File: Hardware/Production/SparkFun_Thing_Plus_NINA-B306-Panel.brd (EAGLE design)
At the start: 22.9 x 66 mm, 145 parts, among them J1 USB-C, J2 THING_PLUS_LOGICAL, J3 CONN_03X2_NO4, J4 MICRO-SDFRICTION, J6 QWIIC_RA, Q1 20V/4.2A/52mΩ/1.4W, Q2 220mA/50V/3.5Ω, Q3 20V/4.2A/52mΩ/1.4W, U1 ESD Diode, U2 U-BLOX_NINA_B306, U3 XC6222B331MR-G, U4 MCP73831, U5 MAX17048, U6 ISM330DHCX, U7 BME280

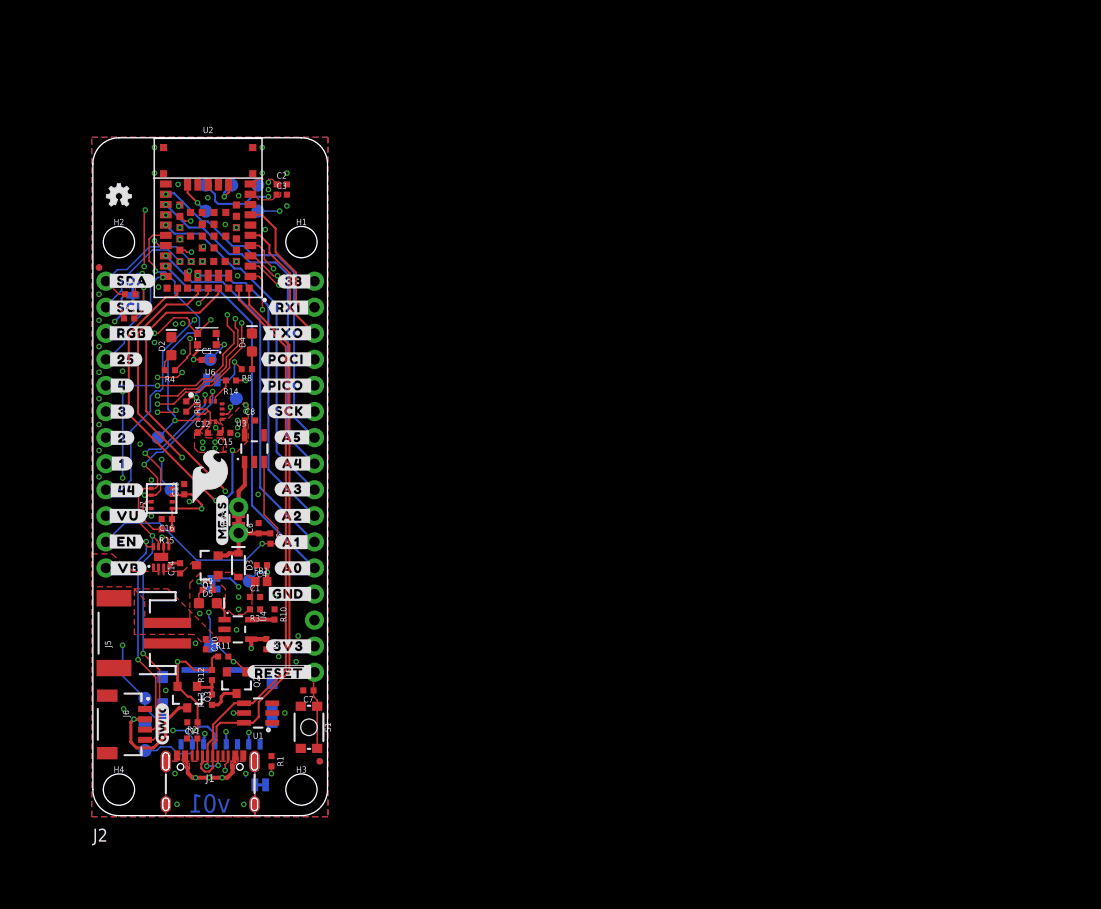
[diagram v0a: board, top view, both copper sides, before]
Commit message: routed and ready for v01 design review.
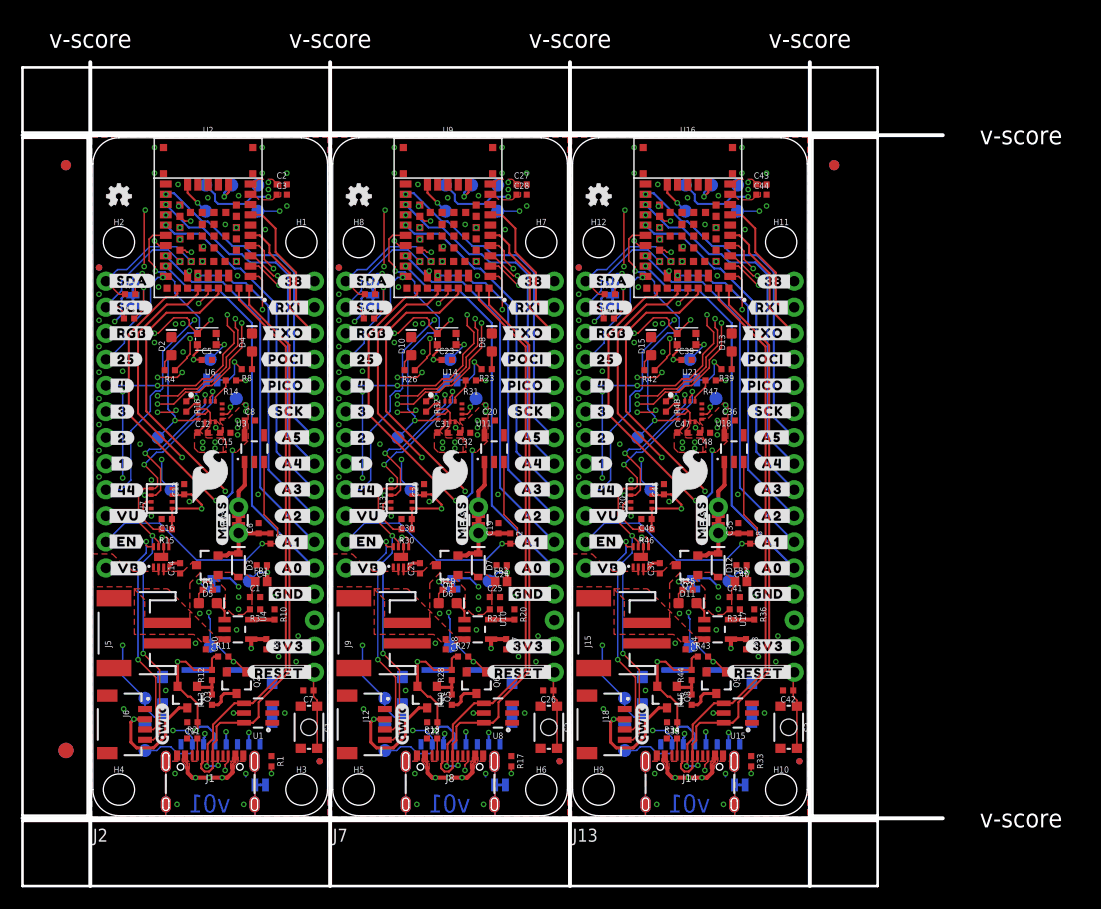
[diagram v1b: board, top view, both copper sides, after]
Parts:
- removed FRAME1: FRAME-LEDGER, SparkFun-Aesthetics:CREATIVE_COMMONS
- added C17, C18, C33, C34: 4.7uF, SparkFun-Capacitors:0402-TIGHT
- added C19, C35: 1.0uF, SparkFun-Capacitors:0402-TIGHT
- added C20, C36: 2.2uF, SparkFun-Capacitors:0402-TIGHT
- added C21, C23, C26, C27, C28, C29, C30, C31, C32, C37, C39, C42, C43, C44, C45, C46, C47, C48: 0.1uF, SparkFun-Capacitors:0402-TIGHT
- added C22, C38: 10uF, SparkFun-Capacitors:0402-TIGHT
- added C24, C25, C40, C41: 1.0nF, SparkFun-Capacitors:0402-TIGHT
- added CHG1, CHG2, PWR1, PWR2: JUMPER-SMT_2_NC_TRACE_SILK, SparkFun-Jumpers:SMT-JUMPER_2_NC_TRACE_SILK
- added D10, D15: BLUE, SparkFun-LED:LED-0603
- added D11, D6: Yellow, SparkFun-LED:LED-0603
- added D12, D7: 3A/10V/280mV, SparkFun-DiscreteSemi:SOD-323
- added D13, D8: RED, SparkFun-LED:LED-0603
- added D14, D9: WS2812, SparkFun-LED:WS2812-2020
- added E$1, E$2, E$3, E$4: (no value), SparkFun-Aesthetics:FIDUCIAL-1X2
- added E$5, E$6: (no value), SparkFun-Retired:FIDUCIAL-1.5X3
- added FB2, FB3: 120Ω, SparkFun-Coils:0402
- added FD10, FD11, FD12, FD5, FD6, FD7, FD8, FD9: FIDUCIALUFIDUCIAL, SparkFun-Aesthetics:FIDUCIAL-MICRO
- added H10, H11, H12, H5, H6, H7, H8, H9: STAND-OFFTIGHT, SparkFun-Hardware:STAND-OFF-TIGHT
- added I2C1, I2C2: JUMPER-SMT_3_2-NC_TRACE_SILK, SparkFun-Jumpers:SMT-JUMPER_3_2-NC_TRACE_SILK
- added J10, J16: MICRO-SDFRICTION, SparkFun-Connectors:MICROSD_TINY
- added J11, J17: CONN_03X2_NO4, MISC:PAD_05_03X2_TP_NO4
- added J12, J18: QWIIC_RA, SparkFun-Connectors:JST04_1MM_RA
- added J13, J7: THING_PLUS_LOGICAL, SparkFun-Boards:THING_PLUS
- added J14, J8: USB-C, SparkFun-Connectors:USB-C-16P-4LAYER-ISOLATED
- added J15, J9: (no value), SparkFun-Connectors:JST-2-SMD
- added LOGO10, LOGO15: FOUR_LAYER_WARNING, SparkFun-Aesthetics:FOUR_LAYER_WARNING
- added LOGO11, LOGO6: SFE_LOGO_NAME_FLAME.1_INCH, SparkFun-Aesthetics:SFE_LOGO_NAME_FLAME_.1
- added LOGO12, LOGO7: OSHW-LOGOMINI, SparkFun-Aesthetics:OSHW-LOGO-MINI
- added LOGO13, LOGO8: SPECIAL_INSTRUCTIONS-ORDERING, SparkFun-Aesthetics:ORDERING_INSTRUCTIONS
- added LOGO14, LOGO9: QWIIC_LOGO_4MM, SparkFun-Aesthetics:QWIIC_4MM
- added MEAS1, MEAS2: JUMPER-COMBO_2_NC_TRACE, SparkFun-Jumpers:COMBO-JUMPER_2_NC_TRACE
- added Q4, Q5, Q7, Q8: 20V/4.2A/52mΩ/1.4W, SparkFun-DiscreteSemi:SOT23-3
- added Q6, Q9: 220mA/50V/3.5Ω, SparkFun-DiscreteSemi:SOT23-3
- added R17, R18, R33, R34: 5.1k, SparkFun-Resistors:0402-TIGHT
- added R19, R35: 4.7k, SparkFun-Resistors:0402-TIGHT
- added R20, R36: 2.0K, SparkFun-Resistors:0402-TIGHT
- added R21, R22, R27, R28, R30, R31, R32, R37, R38, R43, R44, R46, R47, R48: 10k, SparkFun-Resistors:0402-TIGHT
- added R23, R39: 1k, SparkFun-Resistors:0402-TIGHT
- added R24, R25, R26, R40, R41, R42: 2.2k, SparkFun-Resistors:0402-TIGHT
- added R29, R45: 100, SparkFun-Resistors:0402-TIGHT
- added S2, S3: Reset, SparkFun-Switches:TACTILE_SWITCH_SMD_4.6X2.8MM
- added SHLD1, SHLD2: (no value), SparkFun-Jumpers:SMT-JUMPER_2_NC_TRACE_SILK
- added TP10, TP11, TP12, TP13, TP14, TP15, TP16, TP17, TP18, TP19, TP20, TP21, TP22, TP23, TP24, TP25, TP26, TP27: TEST-POINT3X5, SparkFun-Connectors:PAD.03X.05
- added U$100, U$162: (no value), output:#_SCK#71
- added U$101, U$163: (no value), output:#_PICO#72
- added U$102, U$164: (no value), output:#_POCI#73
- added U$103, U$165: (no value), output:#_TXO#74
- added U$104, U$166: (no value), output:#_RXI#75
- added U$105, U$167: (no value), output:#_38#76
- added U$106, U$168: (no value), output:#RGB_#78
- added U$107, U$169: (no value), output:#25_#79
- added U$108, U$170: (no value), output:#4_#79
- added U$109, U$171: (no value), output:#3_#79
- added U$110, U$172: (no value), output:#2_#79
- added U$111, U$173: (no value), output:#1_#79
- added U$112, U$174: (no value), output:#44_#79
- added U$113, U$175: (no value), output:#VUSB_#79
- added U$114, U$176: (no value), output:#EN_#80
- added U$115, U$177: (no value), output:#VBATT_#81
- added U$116, U$178: (no value), output:#SDA_#82
- added U$117, U$179: (no value), output:#SCL_#85
- added U$118, U$180: (no value), output:#_PWR#90
- added U$119, U$181: (no value), output:#CHG_#92
- added U$120, U$182: (no value), output:#_SHLD#93
- added U$121, U$183: (no value), output:SPARKFUN_THING_PLUS96
- added U$122, U$184: (no value), output:NINA#B30697
- added U$123, U$185: (no value), output:#_#RST##30698
- added U$124, U$186: (no value), output:#MEAS#30701
- added U$125, U$63: (no value), SparkFun-Aesthetics:SFE_LOGO_FLAME_STOP_.1
- added U$126, U$64: (no value), SparkFun-Aesthetics:SFE_LOGO_FLAME_.2
- added U$127, U$65: (no value), output:#_VB#46
- added U$128, U$66: (no value), output:#_EN#47
- added U$129, U$67: (no value), output:#_VU#48
- added U$130, U$68: (no value), output:#_44#49
- added U$131, U$69: (no value), output:#_1#49
- added U$132, U$70: (no value), output:#_2#49
- added U$133, U$71: (no value), output:#_3#49
- added U$134, U$72: (no value), output:#_4#49
- added U$135, U$73: (no value), output:#_25#49
- added U$136, U$74: (no value), output:#_SCL#49
- added U$137, U$75: (no value), output:##RESET#_#52
- added U$138, U$76: (no value), output:#GND_#53
- added U$139, U$77: (no value), output:#A0_#54
- added U$140, U$78: (no value), output:#A1_#54
- added U$141, U$79: (no value), output:#A2_#54
- added U$142, U$80: (no value), output:#A3_#54
- added U$143, U$81: (no value), output:#A4_#54
- added U$144, U$82: (no value), output:#A5_#54
- added U$145, U$83: (no value), output:#SCK_#54
- added U$146, U$84: (no value), output:#TXO_#57
- added U$147, U$85: (no value), output:#RXI_#59
- added U$148, U$86: (no value), output:#38_#60
- added U$149, U$87: (no value), output:#PICO_#60
- added U$150, U$88: (no value), output:#POCI_#61
- added U$151, U$89: (no value), output:#_RGB#64
- added U$152, U$90: (no value), output:#3V3_#65
- added U$153, U$91: (no value), output:#_SDA#68
- added U$154, U$92: (no value), output:#_3V3#70
- added U$155, U$93: (no value), output:#_GND#70
- added U$156, U$94: (no value), output:#_A0#71
- added U$157, U$95: (no value), output:#_A1#71
- added U$158, U$96: (no value), output:#_A2#71
- added U$159, U$97: (no value), output:#_A3#71
- added U$160, U$98: (no value), output:#_A4#71
- added U$161, U$99: (no value), output:#_A5#71
- added U10, U17: MCP73831, SparkFun-IC-Power:SOT23-5
- added U11, U18: XC6222B331MR-G, SparkFun-IC-Power:SOT23-5
- added U12, U19: MAX17048, SparkFun-IC-Power:DFN-8
- added U13, U20: BME280, SparkFun-Sensors:LGA-8-2.5X2.5
- added U14, U21: ISM330DHCX, SparkFun-Sensors:LGA-14L
- added U15, U8: ESD Diode, SparkFun-DiscreteSemi:SOT-23-6
- added U16, U9: U-BLOX_NINA_B306, U-BLOX_NINA_B306:NINA_B306
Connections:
- new net !RESET!1: C26.1, J11.6, J7.28, S2.3, S2.4, U9.19
- new net !RESET!2: C42.1, J13.28, J17.6, S3.3, S3.4, U16.19
- new net 3.3V1: C20.1, C22.1, C23.1, C27.1, C28.1, C29.1, C30.1, C31.1, C32.1, D9.VCC, I2C1.2, J10.4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
- new net 3.3V2: C36.1, C38.1, C39.1, C43.1, C44.1, C45.1, C46.1, C47.1, C48.1, D14.VCC, I2C2.2, J13.27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
- new net 3V3_QWIIC1: J12.2, Q5.3, TP18.1
- new net 3V3_QWIIC2: J18.2, Q8.3, TP27.1
- new net EN1: J7.11, R22.2, U11.3
- new net EN2: J13.11, R38.2, U18.3
- new net GND1: C17.2, C18.2, C19.2, C20.2, C21.2, C22.2, C23.2, C24.2, C25.2, C26.2, C27.2, C28.2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
- new net GND2: C33.2, C34.2, C35.2, C36.2, C37.2, C38.2, C39.2, C40.2, C41.2, C42.2, C43.2, C44.2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
- new net IO1/GPIO2: J7.8, U9.1
- new net IO1/GPIO3: J13.8, U16.1
- new net IO17/A1: J7.19, U9.17
- new net IO17/A2: J13.19, U16.17
- new net IO18/A1: J7.20, U9.18
- new net IO18/A2: J13.20, U16.18
- new net IO2/GPIO1: J7.7, U9.2
- new net IO2/GPIO3: J13.7, U16.2
- new net IO20/A1: J7.21, U9.20
- new net IO20/A2: J13.21, U16.20
- new net IO21/IMU_INT2: TP14.1, U14.P4, U9.21
- new net IO21/IMU_INT3: TP23.1, U16.21, U21.P4
- new net IO22/IMU_INT1: TP15.1, U14.P9, U9.22
- new net IO22/IMU_INT3: TP24.1, U16.22, U21.P9
- new net IO23/A2: J7.23, U9.23
- new net IO23/A3: J13.23, U16.23
- new net IO24/A1: J7.24, U9.24
- new net IO24/A2: J13.24, U16.24
- new net IO25/GPIO1: J7.4, U9.25
- new net IO25/GPIO2: J13.4, U16.25
- new net IO27/A1: J7.22, U9.27
- new net IO27/A3: J13.22, U16.27
- new net IO3/GPIO1: J7.6, U9.3
- new net IO3/GPIO2: J13.6, U16.3
- new net IO34/GPIO6/RGB1: D9.DI, J7.3, U9.34
- new net IO34/GPIO6/RGB2: D14.DI, J13.3, U16.34
- new net IO37/SD_DET1: J10.9, TP12.1, U9.37
- new net IO37/SD_DET2: J16.9, TP21.1, U16.37
- new net IO38/FREE1: J7.13, U9.38
- new net IO38/FREE2: J13.13, U16.38
- new net IO39/!BATT_ALRT!1: TP16.1, U12.5, U9.39
- new net IO39/!BATT_ALRT!2: TP25.1, U16.39, U19.5
- new net IO4/GPIO1: J7.5, U9.4
- new net IO4/GPIO2: J13.5, U16.4
- new net IO40/QWIIC_PEN1: Q6.1, R27.2, TP13.1, U9.40
- new net IO40/QWIIC_PEN2: Q9.1, R43.2, TP22.1, U16.40
- new net IO41/LED1: R26.1, U9.41
- new net IO41/LED2: R42.1, U16.41
- new net IO42/SCL1: J12.4, J7.2, R24.1, U12.7, U13.4, U14.P13, U9.42
- new net IO42/SCL2: J13.2, J18.4, R40.1, U16.42, U19.7, U20.4, U21.P13
- new net IO43/SDA1: J12.3, J7.1, R25.1, U12.8, U13.3, U14.P14, U9.43
- new net IO43/SDA2: J13.1, J18.3, R41.1, U16.43, U19.8, U20.3, U21.P14
- new net IO44/GPIO1: J7.9, U9.44
- new net IO44/GPIO2: J13.9, U16.44
- new net IO48/POCI1: J10.7, J7.16, U9.48
- new net IO48/POCI2: J13.16, J16.7, U16.48
- new net IO5/NINA_RX/DEV_TX1: J7.15, U9.5
- new net IO5/NINA_RX/DEV_TX2: J13.15, U16.5
- new net IO50/PICO1: J10.3, J7.17, U9.50
- new net IO50/PICO2: J13.17, J16.3, U16.50
- new net IO51/SD_!CS!1: J10.2, TP10.1, U9.51
- new net IO51/SD_!CS!2: J16.2, TP19.1, U16.51
- new net IO52/SCK1: J10.5, J7.18, U9.52
- new net IO52/SCK2: J13.18, J16.5, U16.52
- new net IO7/NINA_TX/DEV_RX1: J7.14, U9.7
- new net IO7/NINA_TX/DEV_RX2: J13.14, U16.7
- new net N$12: J8.B5, R17.2
- new net N$17: J8.A5, R18.2
- new net N$21: D6.C, U10.1
- new net N$22: D6.A, R19.1
- new net N$23: CHG1.1, R19.2
- new net N$24: R20.2, U10.5
- new net N$25: D8.A, R23.1
- new net N$26: PWR1.1, R23.2
- new net N$27: D9.DO, TP11.1
- new net N$28: C24.1, FB2.2, TP17.1, U9.31
- new net N$29: D10.A, R26.2
- new net N$30: Q6.3, R29.1
- new net N$31: R30.2, U13.2
- new net N$32: R31.2, U14.P12
- new net N$33: R32.2, U14.P1
- new net N$34: Q5.1, R28.1, R29.2
- new net N$35: C19.1, D7.C, MEAS1.1, MEAS1.3, Q4.2, R22.1
- new net N$37: J14.B5, R33.2
- new net N$38: J14.A5, R34.2
- new net N$39: D11.C, U17.1
- new net N$40: D11.A, R35.1
- new net N$41: CHG2.1, R35.2
- new net N$42: R36.2, U17.5
- new net N$43: D13.A, R39.1
- new net N$44: PWR2.1, R39.2
- new net N$45: D14.DO, TP20.1
- new net N$46: C40.1, FB3.2, TP26.1, U16.31
- new net N$47: D15.A, R42.2
- new net N$48: Q9.3, R45.1
- new net N$49: R46.2, U20.2
- new net N$50: R47.2, U21.P12
- new net N$51: R48.2, U21.P1
- new net N$52: Q8.1, R44.1, R45.2
- new net N$53: C35.1, D12.C, MEAS2.1, MEAS2.3, Q7.2, R38.1
- new net SCL_PU_PWR1: I2C1.3, R24.2
- new net SCL_PU_PWR2: I2C2.3, R40.2
- new net SDA_PU_PWR1: I2C1.1, R25.2
- new net SDA_PU_PWR2: I2C2.1, R41.2
- new net SHLD1: J8.SHLD1, J8.SHLD2, J8.SHLD3, J8.SHLD4, J8.SHLD5, J8.SHLD6, J8.SHLD7, J8.SHLD8, SHLD1.2
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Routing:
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- added copper zone on layer 1, net 3.3V1
- added copper zone on layer 15, net 3.3V1
- added copper zone on layer 1, net 3.3V2
- added copper zone on layer 15, net 3.3V2
- added copper zone on layer 1, net GND1
- added copper zone on layer 16, net GND1
- added copper zone on layer 2, net GND1
- added copper zone on layer 1, net GND2
- added copper zone on layer 16, net GND2
- added copper zone on layer 2, net GND2
- added copper zone on layer 1, net SHLD1
- added copper zone on layer 16, net SHLD1
- added copper zone on layer 2, net SHLD1
- added copper zone on layer 1, net SHLD2
- added copper zone on layer 16, net SHLD2
- added copper zone on layer 2, net SHLD2
- added copper zone on layer 1, net V_BATT1
- added copper zone on layer 1, net V_BATT2
- added copper zone on layer 1, net V_USB1
- added copper zone on layer 15, net V_USB1
- added copper zone on layer 1, net V_USB2
- added copper zone on layer 15, net V_USB2
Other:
- board size 22.9 x 66 mm -> 89.7 x 80.3 mm
- board text added: "v-score"
- board text removed: "Alex Brudner"
- board text removed: "All measurements in inches."

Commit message: v01 ready for production.
Move Power LED
Move MEAS jumper
Move GPIO6 to a new IO pin
Remove Q2
Allow ground pour between IO41 and SDA
Add vias next to BME280 ground pad
Shorten !RESET! top silk to !RST!
Swap CHG silk vertical direction
Add IMU silk from ISM BOB
Add more ground vias
Rotate !RST! on bottom silk
Reset button silk
LED silk
Add "NINA-B306" under module on top silk
Align LEDs vertically
Evenly space LEDs horizontally
Reroute
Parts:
- removed Q7, Q8: 20V/4.2A/52mΩ/1.4W, SparkFun-DiscreteSemi:SOT23-3
- removed Q9: 220mA/50V/3.5Ω, SparkFun-DiscreteSemi:SOT23-3
- removed R43, R44, R46, R47, R48: 10k, SparkFun-Resistors:0402-TIGHT
- removed R45: 100, SparkFun-Resistors:0402-TIGHT
- added U$187: (no value), output:#RGB_#78
- added U$188: (no value), output:#25_#79
- added U$189: (no value), output:#4_#79
- added U$190: (no value), output:#3_#79
- added U$191: (no value), output:#2_#79
- added U$192: (no value), output:#1_#79
- added U$193: (no value), output:#44_#79
- added U$194: (no value), output:#VUSB_#79
- added U$195: (no value), output:#EN_#80
- added U$196: (no value), output:#VBATT_#81
- added U$197: (no value), output:#SDA_#82
- added U$198: (no value), output:#SCL_#85
- added U$199: (no value), output:#_PWR#90
- added U$200: (no value), output:#_SHLD#93
- added U$201: (no value), output:SPARKFUN_THING_PLUS96
- added U$202: (no value), output:NINA#B30697
- added U$203: (no value), output:#MEAS#30701
- added U$204: (no value), output:##RST#_#30704
- added U$205: (no value), output:#_#RST##30705
- added U$206: (no value), output:#_CHG#30707
- added U$207: (no value), output:##RESET##30708
- added U$208: (no value), output:RGB30710
- added U$209: (no value), output:STAT30711
- added U$210: (no value), output:PWR30712
- added U$211: (no value), output:NINA#B30630713
- added U$212: (no value), ISMTopMini:X2114
- added U$213: (no value), ISMTopMini:Y2115
- added U$214: (no value), ISMTopMini:Z2116
- added U$215: (no value), output:IO414130630715
- added U$216: (no value), output:IO34414130630716
- D10, D15: value BLUE -> RED
- D13, D8: value RED -> WS2812; device SparkFun-LED:LED-0603 -> SparkFun-LED:WS2812-2020
- D14, D9: value WS2812 -> BLUE; device SparkFun-LED:WS2812-2020 -> SparkFun-LED:LED-0603
- Q2, Q6: value 220mA/50V/3.5Ω -> 20V/4.2A/52mΩ/1.4W
- R11, R30: value 10k -> 5.1k
- R13, R29: value 100 -> 5.1k
- R17: value 5.1k -> 4.7k
- R18: value 5.1k -> 2.0K
- R19: value 4.7k -> 10k
- R20: value 2.0K -> 10k
- R21, R22, R37: value 10k -> 2.2k
- R23: value 1k -> 2.2k
- R24, R25, R26, R40, R41: value 2.2k -> 10k
- R28: value 10k -> 1k
- R31: value 10k -> 4.7k
- R32: value 10k -> 2.0K
- R33, R34: value 5.1k -> 10k
- R35: value 4.7k -> 2.2k
- R36: value 2.0K -> 2.2k
- R39: value 1k -> 10k
- R42: value 2.2k -> 1k
- U$100: device output:#_SCK#71 -> output:#_SDA#68
- U$101: device output:#_PICO#72 -> output:#_3V3#70
- U$102: device output:#_POCI#73 -> output:#_GND#70
- U$103: device output:#_TXO#74 -> output:#_A0#71
- U$104: device output:#_RXI#75 -> output:#_A1#71
- U$105: device output:#_38#76 -> output:#_A2#71
- U$106: device output:#RGB_#78 -> output:#_A3#71
- U$107: device output:#25_#79 -> output:#_A4#71
- U$108: device output:#4_#79 -> output:#_A5#71
- U$109: device output:#3_#79 -> output:#_SCK#71
- U$110: device output:#2_#79 -> output:#_PICO#72
- U$111: device output:#1_#79 -> output:#_POCI#73
- U$112: device output:#44_#79 -> output:#_TXO#74
- U$113: device output:#VUSB_#79 -> output:#_RXI#75
- U$114: device output:#EN_#80 -> output:#_38#76
- U$115: device output:#VBATT_#81 -> output:#RGB_#78
- U$116: device output:#SDA_#82 -> output:#25_#79
- U$117: device output:#SCL_#85 -> output:#4_#79
- U$118: device output:#_PWR#90 -> output:#3_#79
- U$119: device output:#CHG_#92 -> output:#2_#79
- U$120: device output:#_SHLD#93 -> output:#1_#79
- U$121: device output:SPARKFUN_THING_PLUS96 -> output:#44_#79
- U$122: device output:NINA#B30697 -> output:#VUSB_#79
- U$123: device output:#_#RST##30698 -> output:#EN_#80
- U$124: device output:#MEAS#30701 -> output:#VBATT_#81
- U$125: device SparkFun-Aesthetics:SFE_LOGO_FLAME_STOP_.1 -> output:#SDA_#82
- U$126: device SparkFun-Aesthetics:SFE_LOGO_FLAME_.2 -> output:#SCL_#85
- U$127: device output:#_VB#46 -> output:#_PWR#90
- U$128: device output:#_EN#47 -> output:#_SHLD#93
- U$129: device output:#_VU#48 -> output:SPARKFUN_THING_PLUS96
- U$130: device output:#_44#49 -> output:NINA#B30697
- U$131: device output:#_1#49 -> output:#MEAS#30701
- U$132: device output:#_2#49 -> output:##RST#_#30704
- U$133: device output:#_3#49 -> output:#_#RST##30705
- U$134: device output:#_4#49 -> output:#_CHG#30707
- U$135: device output:#_25#49 -> output:##RESET##30708
- U$136: device output:#_SCL#49 -> output:RGB30710
- U$137: device output:##RESET#_#52 -> output:STAT30711
- U$138: device output:#GND_#53 -> output:PWR30712
- U$139: device output:#A0_#54 -> output:NINA#B30630713
- U$140: device output:#A1_#54 -> ISMTopMini:X2114
- U$141: device output:#A2_#54 -> ISMTopMini:Y2115
- U$142: device output:#A3_#54 -> ISMTopMini:Z2116
- U$143: device output:#A4_#54 -> output:IO414130630715
- U$144: device output:#A5_#54 -> output:IO34414130630716
- U$145: device output:#SCK_#54 -> SparkFun-Aesthetics:SFE_LOGO_FLAME_STOP_.1
- U$146: device output:#TXO_#57 -> SparkFun-Aesthetics:SFE_LOGO_FLAME_.2
- U$147: device output:#RXI_#59 -> output:#_VB#46
- U$148: device output:#38_#60 -> output:#_EN#47
- U$149: device output:#PICO_#60 -> output:#_VU#48
- U$15: device output:##RESET#_#52 -> output:##RST#_#30704
- U$150: device output:#POCI_#61 -> output:#_44#49
- U$151: device output:#_RGB#64 -> output:#_1#49
- U$152: device output:#3V3_#65 -> output:#_2#49
- U$153: device output:#_SDA#68 -> output:#_3#49
- U$154: device output:#_3V3#70 -> output:#_4#49
- U$155: device output:#_GND#70 -> output:#_25#49
- U$156: device output:#_A0#71 -> output:#_SCL#49
- U$157: device output:#_A1#71 -> output:#GND_#53
- U$158: device output:#_A2#71 -> output:#A0_#54
- U$159: device output:#_A3#71 -> output:#A1_#54
- U$160: device output:#_A4#71 -> output:#A2_#54
- U$161: device output:#_A5#71 -> output:#A3_#54
- U$162: device output:#_SCK#71 -> output:#A4_#54
- U$163: device output:#_PICO#72 -> output:#A5_#54
- U$164: device output:#_POCI#73 -> output:#SCK_#54
- U$165: device output:#_TXO#74 -> output:#TXO_#57
- U$166: device output:#_RXI#75 -> output:#RXI_#59
- U$167: device output:#_38#76 -> output:#38_#60
- U$168: device output:#RGB_#78 -> output:#PICO_#60
- U$169: device output:#25_#79 -> output:#POCI_#61
- U$170: device output:#4_#79 -> output:#_RGB#64
- U$171: device output:#3_#79 -> output:#3V3_#65
- U$172: device output:#2_#79 -> output:#_SDA#68
- U$173: device output:#1_#79 -> output:#_3V3#70
- U$174: device output:#44_#79 -> output:#_GND#70
- U$175: device output:#VUSB_#79 -> output:#_A0#71
- U$176: device output:#EN_#80 -> output:#_A1#71
- U$177: device output:#VBATT_#81 -> output:#_A2#71
- U$178: device output:#SDA_#82 -> output:#_A3#71
- U$179: device output:#SCL_#85 -> output:#_A4#71
- U$180: device output:#_PWR#90 -> output:#_A5#71
- U$181: device output:#CHG_#92 -> output:#_SCK#71
- U$182: device output:#_SHLD#93 -> output:#_PICO#72
- U$183: device output:SPARKFUN_THING_PLUS96 -> output:#_POCI#73
- U$184: device output:NINA#B30697 -> output:#_TXO#74
- U$185: device output:#_#RST##30698 -> output:#_RXI#75
- U$186: device output:#MEAS#30701 -> output:#_38#76
- U$30: device output:#_#RST##30698 -> output:#_CHG#30707
- U$58: device output:#CHG_#92 -> output:##RESET##30708
- U$63: device SparkFun-Aesthetics:SFE_LOGO_FLAME_STOP_.1 -> output:#_#RST##30705
- U$64: device SparkFun-Aesthetics:SFE_LOGO_FLAME_.2 -> output:RGB30710
- U$65: device output:#_VB#46 -> output:STAT30711
- U$66: device output:#_EN#47 -> output:PWR30712
- U$67: device output:#_VU#48 -> output:NINA#B30630713
- U$68: device output:#_44#49 -> ISMTopMini:X2114
- U$69: device output:#_1#49 -> ISMTopMini:Y2115
- U$70: device output:#_2#49 -> ISMTopMini:Z2116
- U$71: device output:#_3#49 -> output:IO414130630715
- U$72: device output:#_4#49 -> output:IO34414130630716
- U$73: device output:#_25#49 -> SparkFun-Aesthetics:SFE_LOGO_FLAME_STOP_.1
- U$74: device output:#_SCL#49 -> SparkFun-Aesthetics:SFE_LOGO_FLAME_.2
- U$75: device output:##RESET#_#52 -> output:#_VB#46
- U$76: device output:#GND_#53 -> output:#_EN#47
- U$77: device output:#A0_#54 -> output:#_VU#48
- U$78: device output:#A1_#54 -> output:#_44#49
- U$79: device output:#A2_#54 -> output:#_1#49
- U$80: device output:#A3_#54 -> output:#_2#49
- U$81: device output:#A4_#54 -> output:#_3#49
- U$82: device output:#A5_#54 -> output:#_4#49
- U$83: device output:#SCK_#54 -> output:#_25#49
- U$84: device output:#TXO_#57 -> output:#_SCL#49
- U$85: device output:#RXI_#59 -> output:#GND_#53
- U$86: device output:#38_#60 -> output:#A0_#54
- U$87: device output:#PICO_#60 -> output:#A1_#54
- U$88: device output:#POCI_#61 -> output:#A2_#54
- U$89: device output:#_RGB#64 -> output:#A3_#54
- U$90: device output:#3V3_#65 -> output:#A4_#54
- U$91: device output:#_SDA#68 -> output:#A5_#54
- U$92: device output:#_3V3#70 -> output:#SCK_#54
- U$93: device output:#_GND#70 -> output:#TXO_#57
- U$94: device output:#_A0#71 -> output:#RXI_#59
- U$95: device output:#_A1#71 -> output:#38_#60
- U$96: device output:#_A2#71 -> output:#PICO_#60
- U$97: device output:#_A3#71 -> output:#POCI_#61
- U$98: device output:#_A4#71 -> output:#_RGB#64
- U$99: device output:#_A5#71 -> output:#3V3_#65
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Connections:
- removed net IO34/GPIO6/RGB: D1.DI, J2.3, U2.34
- removed net IO34/GPIO6/RGB1: D9.DI, J7.3, U9.34
- removed net IO34/GPIO6/RGB2: D14.DI, J13.3, U16.34
- removed net IO40/QWIIC_PEN: Q2.1, R11.2, TP5.1, U2.40
- removed net IO40/QWIIC_PEN1: Q6.1, R27.2, TP13.1, U9.40
- removed net IO40/QWIIC_PEN2: Q9.1, R43.2, TP22.1, U16.40
- removed net N$23 (its old number): CHG1.1, R19.2
- removed net N$33 (its old number): R32.2, U14.P1
- removed net N$38 (its old number): J14.A5, R34.2
- removed net N$47: D15.A, R42.2
- removed net N$48: Q9.3, R45.1
- removed net N$49: R46.2, U20.2
- removed net N$50: R47.2, U21.P12
- removed net N$51: R48.2, U21.P1
- removed net N$52: Q8.1, R44.1, R45.2
- removed net N$53: C35.1, D12.C, MEAS2.1, MEAS2.3, Q7.2, R38.1
- new net IO34/RGB: D1.DI, U2.34
- new net IO34/RGB1: D8.DI, U9.34
- new net IO34/RGB2: D13.DI, U16.34
- new net IO35/GPIO1: J7.3, U9.35
- new net IO35/GPIO2: J13.3, U16.35
- new net IO35/GPIO6: J2.3, U2.35
- new net IO40/QWIIC_!PEN!: Q3.1, R12.2, TP5.1, U2.40
- new net IO40/QWIIC_!PEN!1: Q4.1, R24.2, TP13.1, U9.40
- new net IO40/QWIIC_!PEN!2: Q6.1, R38.2, TP22.1, U16.40
- new net N$21: R18.2, U10.5
- new net N$28: PWR1.1, R28.2
- new net N$36: R32.2, U17.5
- new net N$39: D14.A, R37.2
- net 3.3V: no longer R11.1, R12.2
- net 3.3V1: now also D8.VCC, Q4.2, R25.1, R26.1; no longer D9.VCC, Q5.2, R28.2, R30.1, R31.1, R32.1
- net 3.3V2: now also D13.VCC, Q6.2, R39.1, R40.1, R41.1; no longer D14.VCC, Q8.2, R43.1, R44.2, R46.1, R47.1, R48.1
- net 3V3_QWIIC1: now also Q4.3; no longer Q5.3
- net 3V3_QWIIC2: now also Q6.3; no longer Q8.3
- net EN1: now also R20.2; no longer R22.2
- net EN2: now also R34.2; no longer R38.2
- net GND: now also R12.1; no longer Q2.2
- net GND1: now also D8.GND, D9.C, R11.1, R13.1, R19.1, R24.1; no longer D8.C, D9.GND, Q6.2, R17.1, R20.1, R21.1
- net GND2: now also D13.GND, D14.C, R29.1, R30.1, R32.1, R38.1; no longer D13.C, D14.GND, Q9.2, R34.1, R36.1, R37.1
- net IO41/LED1: now also R23.1; no longer R26.1
- net IO41/LED2: now also R37.1; no longer R42.1
- net IO42/SCL1: now also R21.1; no longer R24.1
- net IO42/SCL2: now also R35.1; no longer R40.1
- net IO43/SDA1: now also R22.1; no longer R25.1
- net IO43/SDA2: now also R36.1; no longer R41.1
- net N$1: now also J8.B5, R11.2; no longer C6.1, D3.C, MEAS.1, MEAS.3, Q1.2, R6.1
- net N$12: now also D3.C, MEAS.1, MEAS.3, Q1.2; no longer J8.B5, R17.2
- net N$13: now also D6.A, R17.1; no longer Q2.3, R13.1
- net N$17: now also CHG1.1, R17.2; no longer J8.A5, R18.2
- net N$22: now also D8.DO, TP11.1; no longer D6.A, R19.1
- net N$24: now also D9.A, R23.2; no longer R20.2, U10.5
- net N$25: now also R25.2, U13.2; no longer D8.A, R23.1
- net N$26: now also R26.2, U14.P12; no longer PWR1.1, R23.2
- net N$27: now also R27.2, U14.P1; no longer D9.DO, TP11.1
- net N$29: now also R28.1; no longer R26.2
- net N$30: now also D7.C, MEAS1.1, MEAS1.3, Q2.2; no longer Q6.3, R29.1
- net N$31: now also J14.B5, R29.2; no longer R30.2, U13.2
- net N$32: now also J14.A5, R30.2; no longer R31.2, U14.P12
- net N$34: now also D11.A, R31.1; no longer Q5.1, R28.1, R29.2
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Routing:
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
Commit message: Added Layer numbers
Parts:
- added C100, C116, C132, C148, C52, C68, C84: 2.2uF, SparkFun-Capacitors:0402-TIGHT
- added C101, C103, C106, C107, C108, C109, C110, C111, C112, C117, C119, C122, C123, C124, C125, C126, C127, C128, C133, C135, C138, C139, C140, C141, C142, C143, C144, C149, C151, C154, C155, C156, C157, C158, C159, C160, C53, C55, C58, C59, C60, C61, C62, C63, C64, C69, C71, C74, C75, C76, C77, C78, C79, C80, C85, C87, C90, C91, C92, C93, C94, C95, C96: 0.1uF, SparkFun-Capacitors:0402-TIGHT
- added C102, C118, C134, C150, C54, C70, C86: 10uF, SparkFun-Capacitors:0402-TIGHT
- added C104, C105, C120, C121, C136, C137, C152, C153, C56, C57, C72, C73, C88, C89: 1.0nF, SparkFun-Capacitors:0402-TIGHT
- added C113, C114, C129, C130, C145, C146, C49, C50, C65, C66, C81, C82, C97, C98: 4.7uF, SparkFun-Capacitors:0402-TIGHT
- added C115, C131, C147, C51, C67, C83, C99: 1.0uF, SparkFun-Capacitors:0402-TIGHT
- added CHG3, CHG4, CHG5, CHG6, CHG7, CHG8, CHG9, PWR3, PWR4, PWR5, PWR6, PWR7, PWR8, PWR9: JUMPER-SMT_2_NC_TRACE_SILK, SparkFun-Jumpers:SMT-JUMPER_2_NC_TRACE_SILK
- added D16, D21, D26, D31, D36, D41, D46: Yellow, SparkFun-LED:LED-0603
- added D17, D22, D27, D32, D37, D42, D47: 3A/10V/280mV, SparkFun-DiscreteSemi:SOD-323
- added D18, D23, D28, D33, D38, D43, D48: WS2812, SparkFun-LED:WS2812-2020
- added D19, D24, D29, D34, D39, D44, D49: BLUE, SparkFun-LED:LED-0603
- added D20, D25, D30, D35, D40, D45, D50: RED, SparkFun-LED:LED-0603
- added FB10, FB4, FB5, FB6, FB7, FB8, FB9: 120Ω, SparkFun-Coils:0402
- added FD13, FD14, FD15, FD16, FD17, FD18, FD19, FD20, FD21, FD22, FD23, FD24, FD25, FD26, FD27, FD28, FD29, FD30, FD31, FD32, FD33, FD34, FD35, FD36, FD37, FD38, FD39, FD40: FIDUCIALUFIDUCIAL, SparkFun-Aesthetics:FIDUCIAL-MICRO
- added H13, H14, H15, H16, H17, H18, H19, H20, H21, H22, H23, H24, H25, H26, H27, H28, H29, H30, H31, H32, H33, H34, H35, H36, H37, H38, H39, H40: STAND-OFFTIGHT, SparkFun-Hardware:STAND-OFF-TIGHT
- added I2C3, I2C4, I2C5, I2C6, I2C7, I2C8, I2C9: JUMPER-SMT_3_2-NC_TRACE_SILK, SparkFun-Jumpers:SMT-JUMPER_3_2-NC_TRACE_SILK
- added J19, J25, J31, J37, J43, J49, J55: THING_PLUS_LOGICAL, SparkFun-Boards:THING_PLUS
- added J20, J26, J32, J38, J44, J50, J56: USB-C, SparkFun-Connectors:USB-C-16P-4LAYER-ISOLATED
- added J21, J27, J33, J39, J45, J51, J57: (no value), SparkFun-Connectors:JST-2-SMD
- added J22, J28, J34, J40, J46, J52, J58: MICRO-SDFRICTION, SparkFun-Connectors:MICROSD_TINY
- added J23, J29, J35, J41, J47, J53, J59: CONN_03X2_NO4, MISC:PAD_05_03X2_TP_NO4
- added J24, J30, J36, J42, J48, J54, J60: QWIIC_RA, SparkFun-Connectors:JST04_1MM_RA
- added LOGO16, LOGO21, LOGO26, LOGO31, LOGO36, LOGO41, LOGO46: SFE_LOGO_NAME_FLAME.1_INCH, SparkFun-Aesthetics:SFE_LOGO_NAME_FLAME_.1
- added LOGO17, LOGO22, LOGO27, LOGO32, LOGO37, LOGO42, LOGO47: OSHW-LOGOMINI, SparkFun-Aesthetics:OSHW-LOGO-MINI
- added LOGO18, LOGO23, LOGO28, LOGO33, LOGO38, LOGO43, LOGO48: SPECIAL_INSTRUCTIONS-ORDERING, SparkFun-Aesthetics:ORDERING_INSTRUCTIONS
- added LOGO19, LOGO24, LOGO29, LOGO34, LOGO39, LOGO44, LOGO49: QWIIC_LOGO_4MM, SparkFun-Aesthetics:QWIIC_4MM
- added LOGO20, LOGO25, LOGO30, LOGO35, LOGO40, LOGO45, LOGO50: FOUR_LAYER_WARNING, SparkFun-Aesthetics:FOUR_LAYER_WARNING
- added MEAS3, MEAS4, MEAS5, MEAS6, MEAS7, MEAS8, MEAS9: JUMPER-COMBO_2_NC_TRACE, SparkFun-Jumpers:COMBO-JUMPER_2_NC_TRACE
- added Q10, Q7, Q8, Q9: 20V/4.2A/52mΩ/1.4W, SparkFun-DiscreteSemi:SOT23-3
- added R100, R111, R112, R113, R124, R125, R126, R46, R47, R48, R59, R60, R61, R72, R73, R74, R85, R86, R87, R98, R99: 2.2k, SparkFun-Resistors:0402-TIGHT
- added R101, R102, R103, R109, R110, R114, R115, R116, R122, R123, R127, R128, R129, R44, R45, R49, R50, R51, R57, R58, R62, R63, R64, R70, R71, R75, R76, R77, R83, R84, R88, R89, R90, R96, R97: 10k, SparkFun-Resistors:0402-TIGHT
- added R104, R117, R130, R52, R65, R78, R91: 1k, SparkFun-Resistors:0402-TIGHT
- added R105, R106, R118, R119, R53, R54, R66, R67, R79, R80, R92, R93: 5.1k, SparkFun-Resistors:0402-TIGHT
- added R107, R120, R55, R68, R81, R94: 4.7k, SparkFun-Resistors:0402-TIGHT
- added R108, R121, R43, R56, R69, R82, R95: 2.0K, SparkFun-Resistors:0402-TIGHT
- added S10, S4, S5, S6, S7, S8, S9: Reset, SparkFun-Switches:TACTILE_SWITCH_SMD_4.6X2.8MM
- added SHLD3, SHLD4, SHLD5, SHLD6, SHLD7, SHLD8, SHLD9: (no value), SparkFun-Jumpers:SMT-JUMPER_2_NC_TRACE_SILK
- added TP28, TP29, TP30, TP31, TP32, TP33, TP34, TP35, TP36, TP37, TP38, TP39, TP40, TP41, TP42, TP43, TP44, TP45, TP46, TP47, TP48, TP49, TP50, TP51, TP52, TP53, TP54, TP55, TP56, TP57, TP58, TP59, TP60, TP61, TP62, TP63, TP64, TP65, TP66, TP67, TP68, TP69, TP70: TEST-POINT3X5, SparkFun-Connectors:PAD.03X.05
- added U$217, U$292, U$367, U$442, U$517, U$592, U$667, U$742: (no value), output:#_VU#0
- added U$218, U$293, U$368, U$443, U$518, U$593, U$668, U$743: (no value), output:#3V3_#0
- added U$219, U$294, U$369, U$444, U$519, U$594, U$669, U$744: (no value), output:RESET0
- added U$220, U$295, U$370, U$445, U$520, U$595, U$670, U$745: (no value), output:#VUSB_#0
- added U$221, U$296, U$371, U$446, U$521, U$596, U$671, U$746: (no value), output:#VBAT_#0
- added U$222, U$297, U$372, U$447, U$522, U$597, U$672, U$747: (no value), output:#_3V3#0
- added U$223, U$288, U$298, U$363, U$373, U$438, U$448, U$513, U$523, U$588, U$598, U$663, U$673, U$738, U$748: (no value), output:##RST#_#0
- added U$224, U$299, U$374, U$449, U$524, U$599, U$674, U$749: (no value), output:#3
- added U$225, U$300, U$375, U$450, U$525, U$600, U$675, U$750: (no value), output:#4
- added U$226, U$301, U$376, U$451, U$526, U$601, U$676: (no value), SparkFun-Aesthetics:SFE_LOGO_FLAME_STOP_.1
- added U$227, U$302, U$377, U$452, U$527, U$602, U$677: (no value), SparkFun-Aesthetics:SFE_LOGO_FLAME_.2
- added U$228, U$303, U$378, U$453, U$528, U$603, U$678: (no value), output:#_EN#47
- added U$229, U$304, U$379, U$454, U$529, U$604, U$679: (no value), output:#_44#49
- added U$230, U$305, U$380, U$455, U$530, U$605, U$680: (no value), output:#_1#49
- added U$231, U$306, U$381, U$456, U$531, U$606, U$681: (no value), output:#_2#49
- added U$232, U$307, U$382, U$457, U$532, U$607, U$682: (no value), output:#_3#49
- added U$233, U$308, U$383, U$458, U$533, U$608, U$683: (no value), output:#_4#49
- added U$234, U$309, U$384, U$459, U$534, U$609, U$684: (no value), output:#_25#49
- added U$235, U$310, U$385, U$460, U$535, U$610, U$685: (no value), output:#_SCL#49
- added U$236, U$311, U$386, U$461, U$536, U$611, U$686: (no value), output:#GND_#53
- added U$237, U$312, U$387, U$462, U$537, U$612, U$687: (no value), output:#A0_#54
- added U$238, U$313, U$388, U$463, U$538, U$613, U$688: (no value), output:#A1_#54
- added U$239, U$314, U$389, U$464, U$539, U$614, U$689: (no value), output:#A2_#54
- added U$240, U$315, U$390, U$465, U$540, U$615, U$690: (no value), output:#A3_#54
- added U$241, U$316, U$391, U$466, U$541, U$616, U$691: (no value), output:#A4_#54
- added U$242, U$317, U$392, U$467, U$542, U$617, U$692: (no value), output:#A5_#54
- added U$243, U$318, U$393, U$468, U$543, U$618, U$693: (no value), output:#SCK_#54
- added U$244, U$319, U$394, U$469, U$544, U$619, U$694: (no value), output:#TXO_#57
- added U$245, U$320, U$395, U$470, U$545, U$620, U$695: (no value), output:#RXI_#59
- added U$246, U$321, U$396, U$471, U$546, U$621, U$696: (no value), output:#38_#60
- added U$247, U$322, U$397, U$472, U$547, U$622, U$697: (no value), output:#PICO_#60
- added U$248, U$323, U$398, U$473, U$548, U$623, U$698: (no value), output:#POCI_#61
- added U$249, U$324, U$399, U$474, U$549, U$624, U$699: (no value), output:#_SDA#68
- added U$250, U$325, U$400, U$475, U$550, U$625, U$700: (no value), output:#_GND#70
- added U$251, U$326, U$401, U$476, U$551, U$626, U$701: (no value), output:#_A0#71
- added U$252, U$327, U$402, U$477, U$552, U$627, U$702: (no value), output:#_A1#71
- added U$253, U$328, U$403, U$478, U$553, U$628, U$703: (no value), output:#_A2#71
- added U$254, U$329, U$404, U$479, U$554, U$629, U$704: (no value), output:#_A3#71
- added U$255, U$330, U$405, U$480, U$555, U$630, U$705: (no value), output:#_A4#71
- added U$256, U$331, U$406, U$481, U$556, U$631, U$706: (no value), output:#_A5#71
- added U$257, U$332, U$407, U$482, U$557, U$632, U$707: (no value), output:#_SCK#71
- added U$258, U$333, U$408, U$483, U$558, U$633, U$708: (no value), output:#_PICO#72
- added U$259, U$334, U$409, U$484, U$559, U$634, U$709: (no value), output:#_POCI#73
- added U$260, U$335, U$410, U$485, U$560, U$635, U$710: (no value), output:#_TXO#74
- added U$261, U$336, U$411, U$486, U$561, U$636, U$711: (no value), output:#_RXI#75
- added U$262, U$337, U$412, U$487, U$562, U$637, U$712: (no value), output:#_38#76
- added U$263, U$338, U$413, U$488, U$563, U$638, U$713: (no value), output:#25_#79
- added U$264, U$339, U$414, U$489, U$564, U$639, U$714: (no value), output:#4_#79
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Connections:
- removed net 3V3_QWIIC: J6.2, Q3.3, TP6.1
- removed net 3V3_QWIIC1: J12.2, Q4.3, TP18.1
- removed net 3V3_QWIIC2: J18.2, Q6.3, TP27.1
- new net !RESET!3: C58.1, J19.28, J23.6, S4.3, S4.4, U23.19
- new net !RESET!4: C74.1, J25.28, J29.6, S5.3, S5.4, U30.19
- new net !RESET!5: C90.1, J31.28, J35.6, S6.3, S6.4, U37.19
- new net !RESET!6: C106.1, J37.28, J41.6, S7.3, S7.4, U44.19
- new net !RESET!7: C122.1, J43.28, J47.6, S8.3, S8.4, U51.19
- new net !RESET!8: C138.1, J49.28, J53.6, S9.3, S9.4, U58.19
- new net !RESET!9: C154.1, J55.28, J59.6, S10.3, S10.4, U65.19
- new net 3.3V3: C52.1, C54.1, C55.1, C59.1, C60.1, C61.1, C62.1, C63.1, C64.1, D18.VCC, I2C3.2, J19.27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
- new net 3.3V4: C68.1, C70.1, C71.1, C75.1, C76.1, C77.1, C78.1, C79.1, C80.1, D23.VCC, I2C4.2, J25.27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
- new net 3.3V5: C84.1, C86.1, C87.1, C91.1, C92.1, C93.1, C94.1, C95.1, C96.1, D28.VCC, I2C5.2, J31.27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
- new net 3.3V6: C100.1, C102.1, C103.1, C107.1, C108.1, C109.1, C110.1, C111.1, C112.1, D33.VCC, I2C6.2, J37.27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
- new net 3.3V7: C116.1, C118.1, C119.1, C123.1, C124.1, C125.1, C126.1, C127.1, C128.1, D38.VCC, I2C7.2, J43.27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
- new net 3.3V8: C132.1, C134.1, C135.1, C139.1, C140.1, C141.1, C142.1, C143.1, C144.1, D43.VCC, I2C8.2, J49.27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
- new net 3.3V9: C148.1, C150.1, C151.1, C155.1, C156.1, C157.1, C158.1, C159.1, C160.1, D48.VCC, I2C9.2, J55.27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
- new net EN3: J19.11, R45.2, U25.3
- new net EN4: J25.11, R58.2, U32.3
- new net EN5: J31.11, R71.2, U39.3
- new net EN6: J37.11, R84.2, U46.3
- new net EN7: J43.11, R97.2, U53.3
- new net EN8: J49.11, R110.2, U60.3
- new net EN9: J55.11, R123.2, U67.3
- new net GND3: C49.2, C50.2, C51.2, C52.2, C53.2, C54.2, C55.2, C56.2, C57.2, C58.2, C59.2, C60.2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
- new net GND4: C65.2, C66.2, C67.2, C68.2, C69.2, C70.2, C71.2, C72.2, C73.2, C74.2, C75.2, C76.2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
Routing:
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- added copper zone on layer 1, net 3.3V3
- added copper zone on layer 15, net 3.3V3
- added copper zone on layer 1, net 3.3V4
- added copper zone on layer 15, net 3.3V4
- added copper zone on layer 1, net 3.3V5
- added copper zone on layer 15, net 3.3V5
- added copper zone on layer 1, net 3.3V6
- added copper zone on layer 15, net 3.3V6
- added copper zone on layer 1, net 3.3V7
- added copper zone on layer 15, net 3.3V7
- added copper zone on layer 1, net 3.3V8
- added copper zone on layer 15, net 3.3V8
- added copper zone on layer 1, net 3.3V9
- added copper zone on layer 15, net 3.3V9
- added copper zone on layer 1, net GND3
- added copper zone on layer 16, net GND3
- added copper zone on layer 2, net GND3
- added copper zone on layer 1, net GND4
- added copper zone on layer 16, net GND4
- added copper zone on layer 2, net GND4
- added copper zone on layer 1, net GND5
- added copper zone on layer 16, net GND5
- added copper zone on layer 2, net GND5
- added copper zone on layer 1, net GND6
- added copper zone on layer 16, net GND6
- added copper zone on layer 2, net GND6
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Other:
- board size 89.7 x 80.3 mm -> 130 x 157 mm
- board text added: "1"
- board text added: "2"
- board text added: "3"
- board text added: "4"
- board text added: "Route Out"
- board text added: "v10"
- board text removed: "v01"
